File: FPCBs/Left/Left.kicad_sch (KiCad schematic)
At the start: 7 parts, among them J1 Conn_01x02_Pin, SW1 SW_Rotary_1x6_MP

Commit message: Add connector
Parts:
- J1: footprint Connector_Coaxial:WR-MMCX_Wuerth_66012102111404_Vertical -> Leica-G9ii:FPC-2Rows-27Pins-0.23mm
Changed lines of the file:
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@@
 			)
 		)
-		(property "Footprint" "Connector_Coaxial:WR-MMCX_Wuerth_66012102111404_Vertical"
+		(property "Footprint" "Leica-G9ii:FPC-2Rows-27Pins-0.23mm"
 			(at 53.34 101.6 0)
 			(effects

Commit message: Update to kicad 9
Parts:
- J1: value Conn_01x02_Pin -> To PCB; footprint Leica-G9ii:FPC-2Rows-27Pins-0.23mm -> Leica-G9ii:FPC-2Rows-27Pins-0.5mm
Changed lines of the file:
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@@
 (kicad_sch
-	(version 20231120)
+	(version 20250114)
 	(generator "eeschema")
-	(generator_version "8.0")
+	(generator_version "9.0")
 	(paper "A4")
 	(junction
@@
 			)
 		)
-		(property "Value" "Conn_01x02_Pin"
+		(property "Value" "To PCB"
 			(at 53.975 99.06 0)
 			(effects
@@
 			)
 		)
-		(property "Footprint" "Leica-G9ii:FPC-2Rows-27Pins-0.23mm"
+		(property "Footprint" "Leica-G9ii:FPC-2Rows-27Pins-0.5mm"
 			(at 53.34 101.6 0)
 			(effects
@@
 		)
 	)
+	(embedded_fonts no)
 )

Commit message: Fixes on the left side FPC
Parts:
- R1, R2, R3, R4, R5: footprint Resistor_SMD:R_0201_0603Metric -> Leica-G9ii:R_2x1mm
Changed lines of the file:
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@@
 			)
 		)
-		(property "Footprint" "Resistor_SMD:R_0201_0603Metric"
+		(property "Footprint" "Leica-G9ii:R_2x1mm"
 			(at 103.632 106.68 90)
 			(effects
@@
 			)
 		)
-		(property "Footprint" "Resistor_SMD:R_0201_0603Metric"
+		(property "Footprint" "Leica-G9ii:R_2x1mm"
 			(at 103.632 99.06 90)
 			(effects
@@
 			)
 		)
-		(property "Footprint" "Resistor_SMD:R_0201_0603Metric"
+		(property "Footprint" "Leica-G9ii:R_2x1mm"
 			(at 103.632 114.3 90)
 			(effects
@@
 			)
 		)
-		(property "Footprint" "Resistor_SMD:R_0201_0603Metric"
+		(property "Footprint" "Leica-G9ii:R_2x1mm"
 			(at 103.632 121.92 90)
 			(effects
@@
 			)
 		)
-		(property "Footprint" "Resistor_SMD:R_0201_0603Metric"
+		(property "Footprint" "Leica-G9ii:R_2x1mm"
 			(at 103.632 91.44 90)
 			(effects

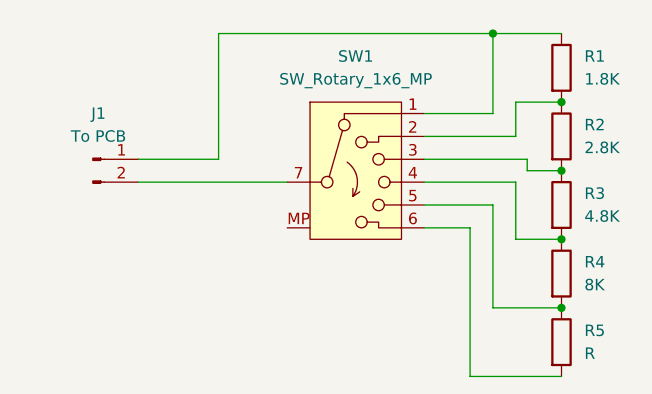
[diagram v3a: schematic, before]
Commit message: Add Canon shutter footprint
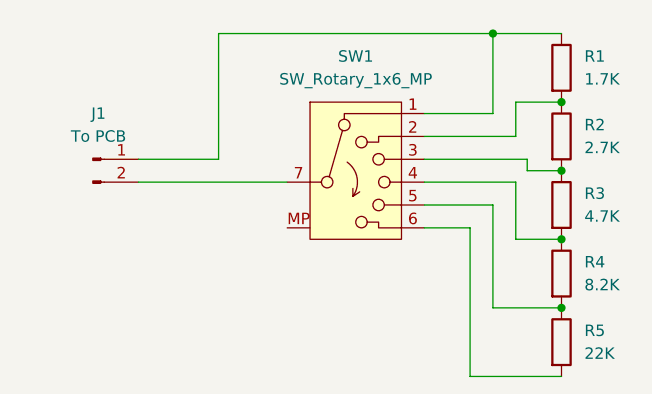
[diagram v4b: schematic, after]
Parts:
- R1: value 1.8K -> 1.7K
- R2: value 2.8K -> 2.7K
- R3: value 4.8K -> 4.7K
- R4: value 8K -> 8.2K
- R5: value R -> 22K
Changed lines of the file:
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@@
 			)
 		)
-		(property "Value" "4.8K"
+		(property "Value" "4.7K"
 			(at 107.95 107.9499 0)
 			(effects
@@
 			)
 		)
-		(property "Value" "2.8K"
+		(property "Value" "2.7K"
 			(at 107.95 100.3299 0)
 			(effects
@@
 			)
 		)
-		(property "Value" "8K"
+		(property "Value" "8.2K"
 			(at 107.95 115.5699 0)
 			(effects
@@
 			)
 		)
-		(property "Value" "R"
+		(property "Value" "22K"
 			(at 107.95 123.1899 0)
 			(effects
@@
 			)
 		)
-		(property "Value" "1.8K"
+		(property "Value" "1.7K"
 			(at 107.95 92.7099 0)
 			(effects

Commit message: Fix left fpcb
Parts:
- R1, R2, R3, R4, R5: footprint Leica-G9ii:R_2x1mm -> Leica-G9ii:R_0603
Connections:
- net at R1.1, SW1.1: now also J1.2 (Pin_2); no longer J1.1 (Pin_1)
- net at SW1.7: now also J1.1 (Pin_1); no longer J1.2 (Pin_2)
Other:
- moved on the sheet: J1, R1, R2, R3, R4, R5
